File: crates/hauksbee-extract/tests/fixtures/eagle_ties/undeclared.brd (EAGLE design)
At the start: 0 parts

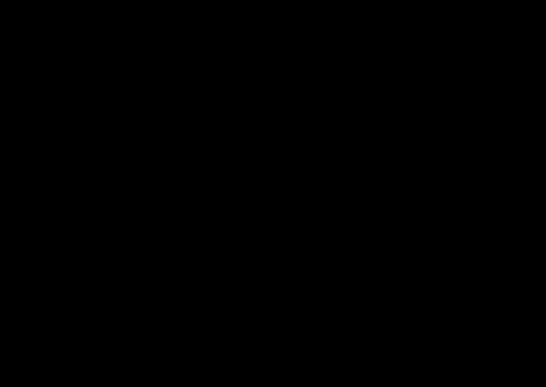
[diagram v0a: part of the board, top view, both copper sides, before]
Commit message: Fix Eagle schematic net-tie parity
Require physical vertical copper and canonical pin/net identity before qualifying Eagle contacts. Preserve the established APIs while carrying optional schematic evidence through CLI, TUI, reports, standalone web analysis, and live launch.
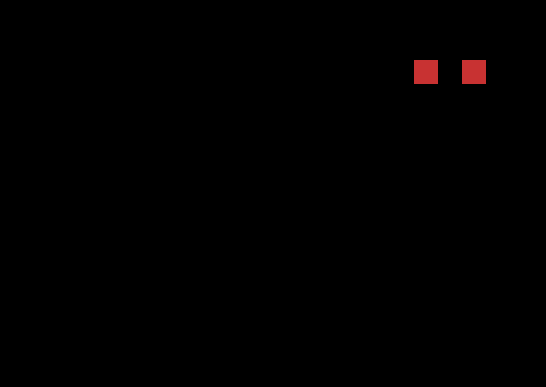
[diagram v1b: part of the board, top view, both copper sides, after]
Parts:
- added R1: 10k, device:R0603
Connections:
- new net AGND: R1.2
- new net GND: R1.1
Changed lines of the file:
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@@
 <?xml version="1.0"?>
-<eagle version="6.6.0"><drawing><layers><layer number="1" name="Top"/></layers><board><libraries/><designrules name="default">
+<eagle version="6.6.0"><drawing><layers><layer number="1" name="Top"/></layers><board><designrules name="default">
 <param name="mdWireWire" value="6mil"/><param name="mdWirePad" value="6mil"/><param name="mdPadPad" value="6mil"/><param name="mdSmdSmd" value="6mil"/>
-</designrules><elements/><signals><signal name="GND"><wire x1="0" y1="0" x2="10" y2="0" width="0.5" layer="1"/></signal><signal name="AGND"><wire x1="5" y1="-5" x2="5" y2="5" width="0.5" layer="1"/></signal></signals></board></drawing></eagle>
+</designrules><elements><element name="R1" library="device" package="R0603" value="10k" x="20" y="20"/></elements><signals><signal name="GND"><contactref element="R1" pad="1"/><wire x1="0" y1="0" x2="10" y2="0" width="0.5" layer="1"/></signal><signal name="AGND"><contactref element="R1" pad="2"/><wire x1="5" y1="-5" x2="5" y2="5" width="0.5" layer="1"/></signal></signals></board></drawing></eagle>
